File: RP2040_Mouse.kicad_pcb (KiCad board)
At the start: 2 copper layers, 54.6 x 30.8 mm, 43 parts, among them J1 DB9_Male, J2 Barrel_Jack_Switch, J3 USB_A, Q1 Q_NPN_BEC, SW1 SW_DPDT_x2, U1 LSF0108PWR, U2 RP2040, U3 AT25SF081B-SSHD-T, U4 AMS1117-3.3, Y1 12MHZ

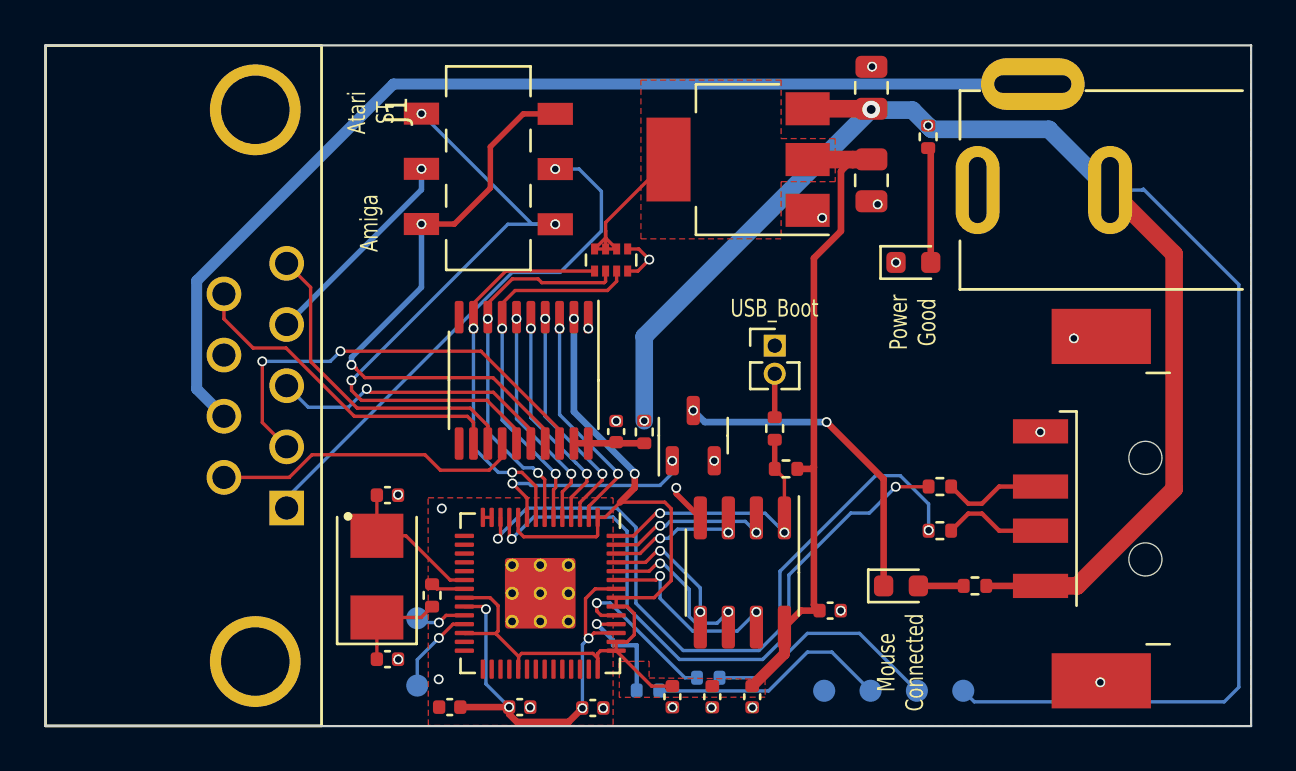
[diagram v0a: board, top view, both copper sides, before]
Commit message: Rev 6
Fully rerouted the board to make it cheaper and easier to make at PCBWay
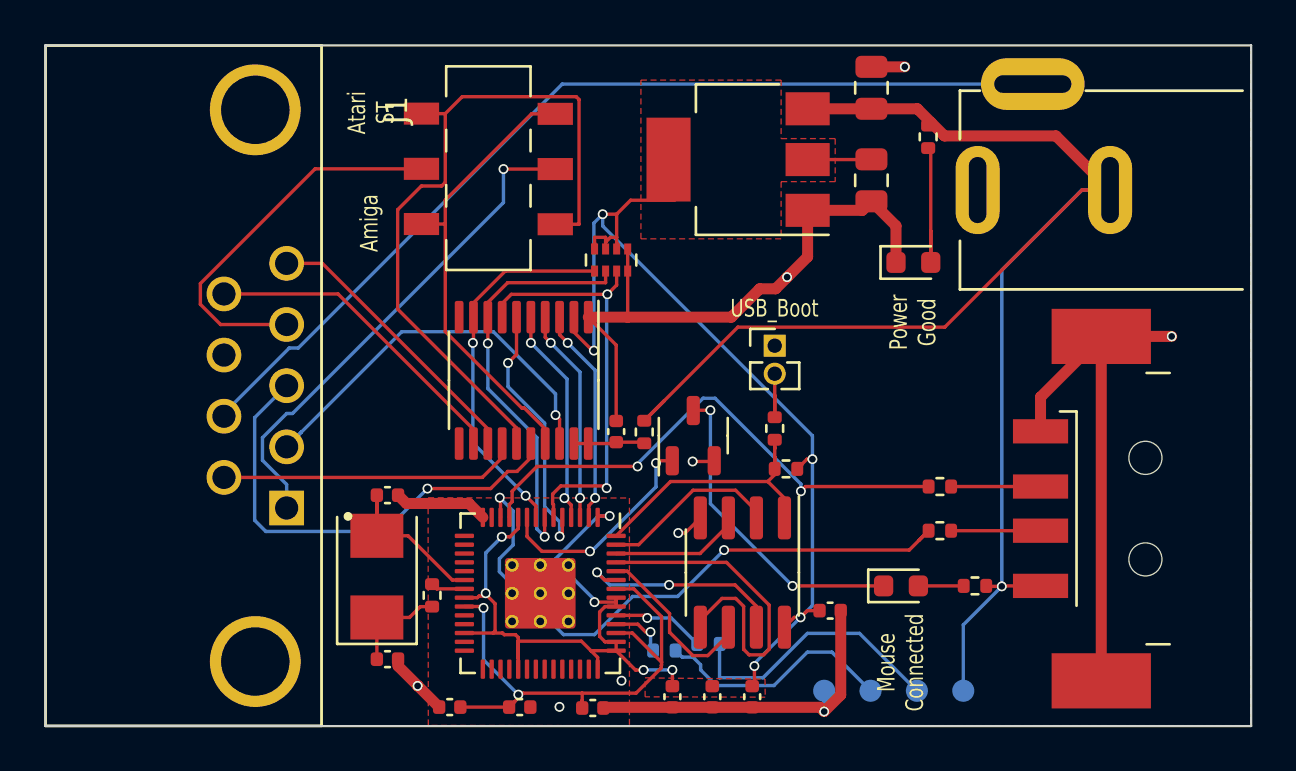
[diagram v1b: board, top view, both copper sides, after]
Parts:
- removed TP1: SWD, TestPoint:TestPoint_Pad_D1.0mm
- removed TP2: SWCLK, TestPoint:TestPoint_Pad_D1.0mm
- moved R10 1.96 mm to (145.8, 120.2)
- moved R9 1.53 mm to (147.8, 119.9)
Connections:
- U2 pad 24: /Microcontroller/SWCLK -> unconnected-(U2-SWCLK-Pad24)
- U2 pad 25: /Microcontroller/SWD -> unconnected-(U2-SWD-Pad25)
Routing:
- net GND: track 4.59 -> 79.4 mm, vias 22 -> 9
- net +5V: track 97.5 -> 71.0 mm, vias 3 -> 1
- net QSPI_SD0: track 5.81 -> 16.0 mm, vias 2 -> 0
- net YA_5: track 13.2 -> 21.8 mm
- net Pin4: track 9.58 -> 17.4 mm, vias 1 -> 0
- net XB_5: track 27.3 -> 21.0 mm, vias 2 -> 0
- net /Microcontroller/USB_T_D+: track 29.8 -> 23.9 mm
- net DB9_5V: track 48.2 -> 43.0 mm
- net +1V1: track 20.2 -> 24.3 mm, vias 4 -> 2
- net /Microcontroller/SWD: track 3.97 -> 0.00 mm, vias 1 -> 0
- net /Microcontroller/USB_T_D-: track 32.4 -> 28.9 mm
- net ML: track 16.3 -> 19.6 mm
- net YB_5: track 29.6 -> 32.8 mm, vias 3 -> 0
- net Net-(U2-USB_DP): track 7.27 -> 4.21 mm
- net Net-(U2-USB_DM): track 5.28 -> 2.59 mm
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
